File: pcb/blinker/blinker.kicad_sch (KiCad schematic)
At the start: 14 parts, among them J1 Conn_01x04_Pin, J2 Conn_01x02_Pin_for_flashing, J3 Screw_Terminal_01x04, Q1 BC547, SW2 SW_MEC_5E, U1 ESP-12F

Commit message: Replace 0402 resistors with 2012 handSolder
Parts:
- R1, R2, R3, R4, R5, R6: footprint Resistor_SMD:R_01005_0402Metric -> Resistor_SMD:R_0805_2012Metric_Pad1.20x1.40mm_HandSolder
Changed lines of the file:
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@@
 			)
 		)
-		(property "Footprint" "Resistor_SMD:R_01005_0402Metric"
+		(property "Footprint" "Resistor_SMD:R_0805_2012Metric_Pad1.20x1.40mm_HandSolder"
 			(at 133.858 104.14 90)
 			(hide yes)
@@
 			)
 		)
-		(property "Footprint" "Resistor_SMD:R_01005_0402Metric"
+		(property "Footprint" "Resistor_SMD:R_0805_2012Metric_Pad1.20x1.40mm_HandSolder"
 			(at 163.068 72.39 90)
 			(hide yes)
@@
 			)
 		)
-		(property "Footprint" "Resistor_SMD:R_01005_0402Metric"
+		(property "Footprint" "Resistor_SMD:R_0805_2012Metric_Pad1.20x1.40mm_HandSolder"
 			(at 128.27 84.582 90)
 			(hide yes)
@@
 			)
 		)
-		(property "Footprint" "Resistor_SMD:R_01005_0402Metric"
+		(property "Footprint" "Resistor_SMD:R_0805_2012Metric_Pad1.20x1.40mm_HandSolder"
 			(at 122.428 72.39 90)
 			(hide yes)
@@
 			)
 		)
-		(property "Footprint" "Resistor_SMD:R_01005_0402Metric"
+		(property "Footprint" "Resistor_SMD:R_0805_2012Metric_Pad1.20x1.40mm_HandSolder"
 			(at 121.158 115.57 90)
 			(hide yes)
@@
 			)
 		)
-		(property "Footprint" "Resistor_SMD:R_01005_0402Metric"
+		(property "Footprint" "Resistor_SMD:R_0805_2012Metric_Pad1.20x1.40mm_HandSolder"
 			(at 77.978 74.93 90)
 			(hide yes)

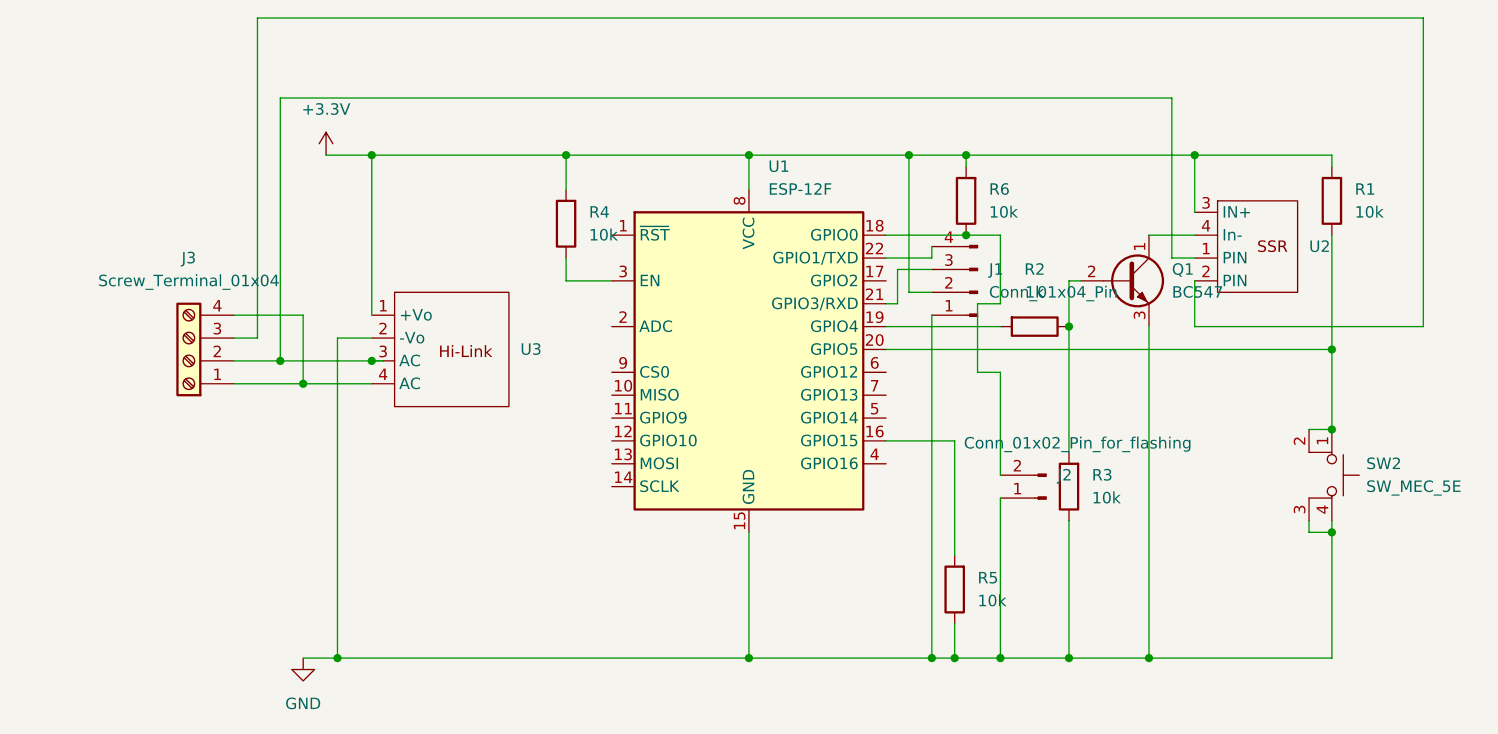
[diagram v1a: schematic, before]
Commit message: Change to Converter_ACDC:HLK-5M03
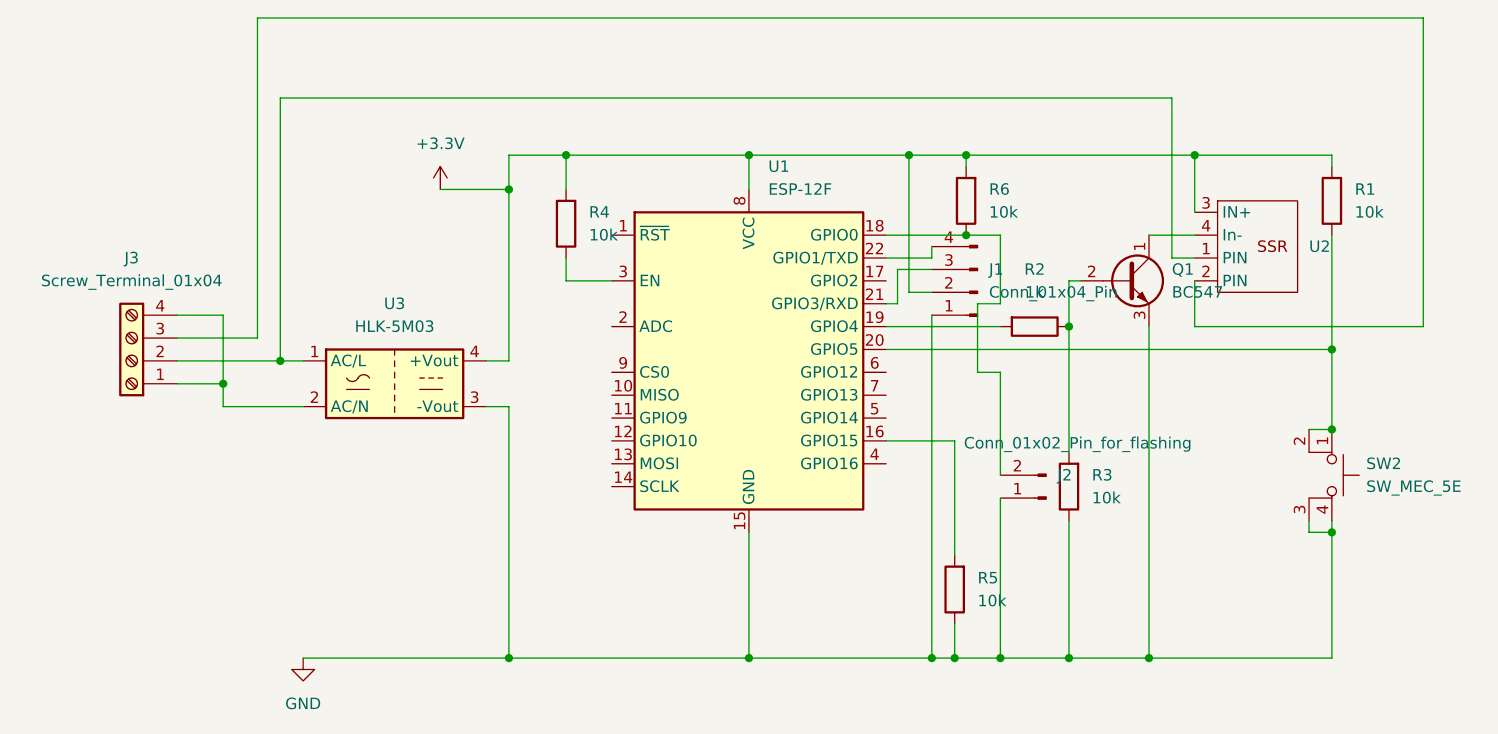
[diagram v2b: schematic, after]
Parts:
- removed U3: (no value), Converter_ACDC:Converter_ACDC_Hi-Link_HLK-5Mxx, symbol CustomRelay:Hi-Link
- added U3: HLK-5M03, Converter_ACDC:Converter_ACDC_Hi-Link_HLK-5Mxx, symbol Converter_ACDC:HLK-5M03
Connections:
- net +3.3V: now also U3.4 (+Vout)
- net GND: now also U3.3 (-Vout)
- net at J3.2 (Pin_2), U2.1 (PIN): now also U3.1 (AC/L)
- net at J3.1 (Pin_1), J3.4 (Pin_4): now also U3.2 (AC/N)
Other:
- moved on the sheet: J3
